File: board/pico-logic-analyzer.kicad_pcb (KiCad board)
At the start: 4 copper layers, 85 x 57.5 mm, 67 parts, among them J1 Conn_02x03_Odd_Even, J10 Conn_02x03_Odd_Even, J11 Conn_01x01, J2 Conn_02x03_Odd_Even, J3 Conn_02x03_Odd_Even, J4 Conn_02x03_Odd_Even, J5 Conn_02x03_Odd_Even, J6 Conn_02x03_Odd_Even, J7 Conn_02x03_Odd_Even, J8 Conn_02x03_Odd_Even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

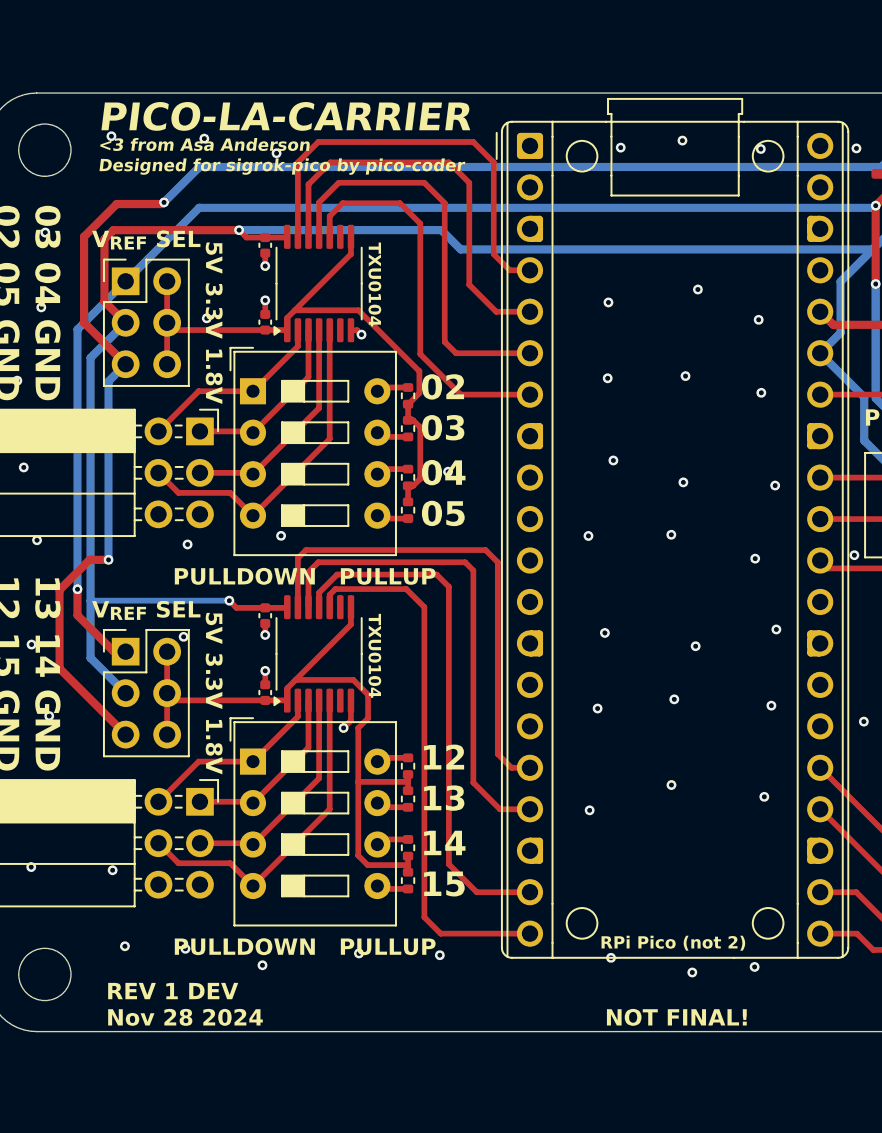
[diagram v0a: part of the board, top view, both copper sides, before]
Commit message: silkscreen cleanups
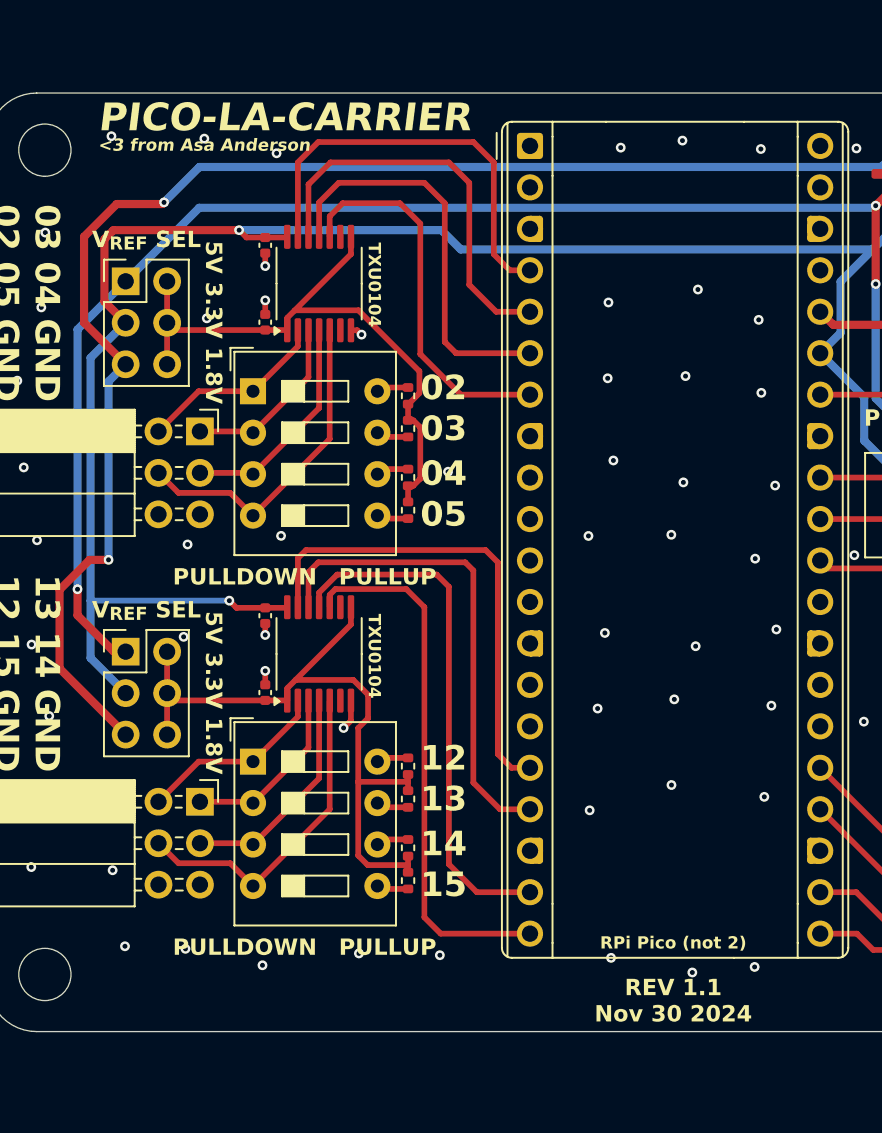
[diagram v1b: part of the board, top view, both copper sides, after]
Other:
- board text added: "REV 1.1 Nov 30 2024"
- board text added: "github.com/tandej/pico-logic-analyzer github.com/pico-coder/sigrok-pico github.com/recursivenomad/ki-lime-pi-to-go"
- board text removed: "DEV NOTES"
- board text removed: "Designed for sigrok-pico by pico-coder"
- board text removed: "NOT FINAL!"
- board text removed: "REV 1 DEV Nov 28 2024"
- board text removed: "Uses recursivenomad's ki-lime-pi-to-go"
